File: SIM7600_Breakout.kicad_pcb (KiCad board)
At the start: 4 copper layers, 40 x 80 mm, 67 parts, among them J1 SIM8060-6-0-14-00-A, J2 2H header, J3 MJ-3502N, J4 30H Header, J5 USB_B_Micro, J6 U.FL-R-SMT-1(01), J7 U.FL-R-SMT-1(01), J8 U.FL-R-SMT-1(01), Q1 MMBT3904L_RFG, U1 NVT2008PW_118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

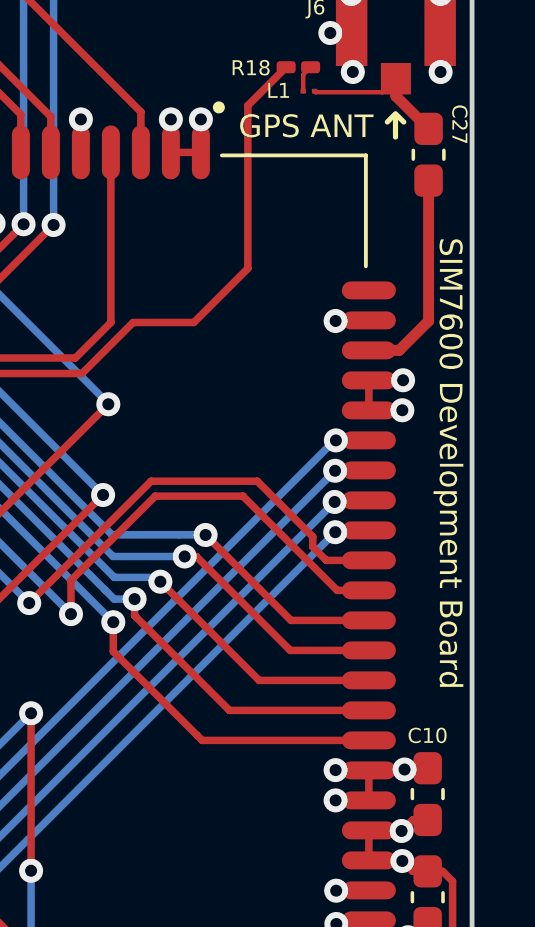
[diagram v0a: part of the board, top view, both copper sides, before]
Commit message: PCB label update
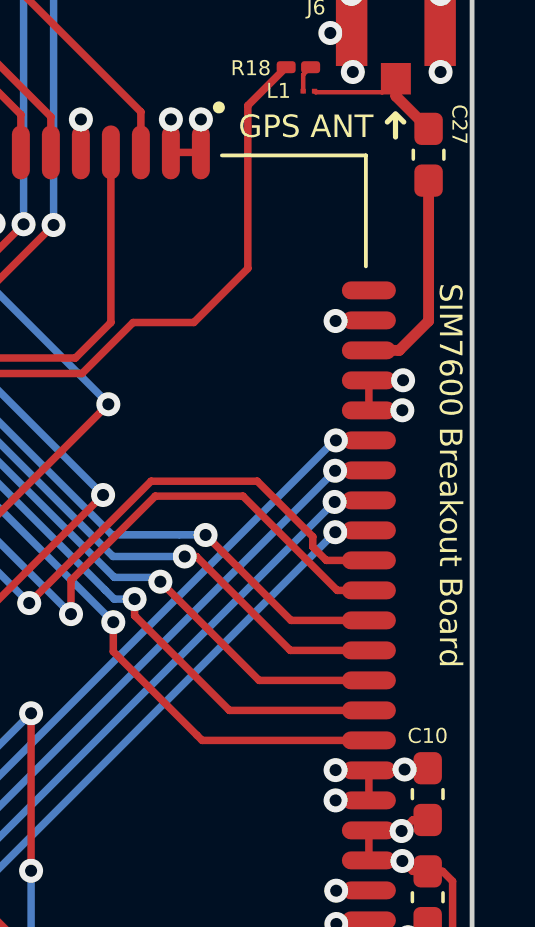
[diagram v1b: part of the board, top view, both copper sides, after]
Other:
- board text added: "SIM7600 Breakout Board"
- board text removed: "SIM7600 Development Board"
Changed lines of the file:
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@@
     (effects (font (size 0.5 0.5) (thickness 0.125)))
   )
-  (gr_text "SIM7600 Development Board" (at 158.275 100.3 270) (layer "F.SilkS")
+  (gr_text "SIM7600 Breakout Board" (at 158.275 100.7 270) (layer "F.SilkS")
     (effects (font (size 0.75 0.75) (thickness 0.15)))
   )

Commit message: Minor fixes
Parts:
- J2: value 2H header -> 2W Header
- J4: value 30H Header -> 30W Header
- U3: value SIM7600 -> SIM7600G-H
- turned R8 to 180 degrees
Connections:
- D3 pad C: /D+ -> /D-
- D4 pad C: /D- -> /D+
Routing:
- net /GPIO77: track 79.3 -> 78.3 mm
- net /+3v3: track 38.6 -> 37.7 mm
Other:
- rule pad_to_mask_clearance: 0 -> 0.0508
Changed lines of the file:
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@@
       (dielectric_constraints no)
     )
-    (pad_to_mask_clearance 0)
+    (pad_to_mask_clearance 0.0508)
     (pcbplotparams
       (layerselection 0x00010fc_ffffffff)
@@
       (effects (font (size 0.5 0.5) (thickness 0.075)))
     )
-    (fp_text value "SIM7600" (at -6.745 17.265 -270) (layer "F.Fab")
+    (fp_text value "SIM7600G-H" (at -6.745 17.265 -270) (layer "F.Fab")
       (effects (font (size 1 1) (thickness 0.15)))
     )
@@
       (effects (font (size 0.5 0.5) (thickness 0.075)))
     )
-    (fp_text value "2H header" (at 0 4.87 90) (layer "F.Fab")
+    (fp_text value "2W Header" (at 0 4.87 90) (layer "F.Fab")
       (effects (font (size 1 1) (thickness 0.15)))
     )
@@
       (net 2 "GND") (pintype "passive"))
     (pad "C" smd rect (at -0.58 0 90) (size 0.94 0.2) (layers "F.Cu" "F.Paste" "F.Mask")
-      (net 112 "/D-") (pintype "passive"))
+      (net 93 "/D+") (pintype "passive"))
     (model "${KIPRJMOD}/3dmodels/ESD9L5.0ST5G.step"
       (offset (xyz 0 0 0))
@@
       (net 2 "GND") (pintype "passive"))
     (pad "C" smd rect (at -0.58 0 90) (size 0.94 0.2) (layers "F.Cu" "F.Paste" "F.Mask")
-      (net 93 "/D+") (pintype "passive"))
+      (net 112 "/D-") (pintype "passive"))
     (model "${KIPRJMOD}/3dmodels/ESD9L5.0ST5G.step"
       (offset (xyz 0 0 0))
@@
   )
   (footprint "Resistor_SMD:R_0201_0603Metric_Pad0.64x0.40mm_HandSolder" (layer "F.Cu")
-    (at 125.0975 66.24)
+    (at 125.0975 66.24 180)
     (descr "Resistor SMD 0201 (0603 Metric), square (rectangular) end terminal, IPC_7351 nominal with elongated pad for handsoldering. (Body size source: https://www.vishay.com/docs/20052/crcw0201e3.pdf), generated with kicad-footprint-generator")
     (tags "resistor handsolder")
@@
     (property "Sheetname" "")
     (attr smd)
-    (fp_text reference "R8" (at 0 -0.665 unlocked) (layer "F.SilkS")
+    (fp_text reference "R8" (at 0 0.69 unlocked) (layer "F.SilkS")
       (effects (font (size 0.5 0.5) (thickness 0.075)))
     )
@@
     (fp_line (start -0.3 -0.15) (end 0.3 -0.15) (layer "F.Fab") (width 0.1))
     (fp_line (start -0.3 0.15) (end -0.3 -0.15) (layer "F.Fab") (width 0.1))
-    (pad "" smd roundrect (at -0.4325 0) (size 0.458 0.36) (layers "F.Paste") (roundrect_rratio 0.25))
-    (pad "" smd roundrect (at 0.4325 0) (size 0.458 0.36) (layers "F.Paste") (roundrect_rratio 0.25))
-    (pad "1" smd roundrect (at -0.4075 0) (size 0.635 0.4) (layers "F.Cu" "F.Mask") (roundrect_rratio 0.25)
+    (pad "" smd roundrect (at -0.4325 0 180) (size 0.458 0.36) (layers "F.Paste") (roundrect_rratio 0.25))
+    (pad "" smd roundrect (at 0.4325 0 180) (size 0.458 0.36) (layers "F.Paste") (roundrect_rratio 0.25))
+    (pad "1" smd roundrect (at -0.4075 0 180) (size 0.635 0.4) (layers "F.Cu" "F.Mask") (roundrect_rratio 0.25)
       (net 3 "Net-(Q1-Pad1)") (pintype "passive"))
-    (pad "2" smd roundrect (at 0.4075 0) (size 0.635 0.4) (layers "F.Cu" "F.Mask") (roundrect_rratio 0.25)
+    (pad "2" smd roundrect (at 0.4075 0 180) (size 0.635 0.4) (layers "F.Cu" "F.Mask") (roundrect_rratio 0.25)
       (net 90 "/PWR_ON") (pintype "passive"))
     (model "${KICAD6_3DMODEL_DIR}/Resistor_SMD.3dshapes/R_0201_0603Metric.wrl"
@@
       (effects (font (size 1 1) (thickness 0.15)) (justify mirror))
     )
-    (fp_text value "30H Header" (at 0 -75.99) (layer "B.Fab")
+    (fp_text value "30W Header" (at 0 -75.99) (layer "B.Fab")
       (effects (font (size 1 1) (thickness 0.15)) (justify mirror))
     )
@@
   (segment (start 154.985 87.21) (end 155.025 87.25) (width 0.3628) (layer "F.Cu") (net 2))
   (segment (start 157.55 70.465) (end 157.55 69.625) (width 0.25) (layer "F.Cu") (net 2))
-  (segment (start 155.6325 110.4575) (end 155.56 110.53) (width 0.25) (layer "F.Cu") (net 2))
   (segment (start 149.93 118.6) (end 148.96 118.6) (width 0.25) (layer "F.Cu") (net 2))
   (segment (start 132.96 120.13) (end 132.96 121.22) (width 0.25) (layer "F.Cu") (net 2))
@@
   (via (at 144.55 121.87) (size 0.8) (drill 0.4) (layers "F.Cu" "B.Cu") (net 2))
   (via (at 151.15 122.85) (size 0.8) (drill 0.4) (layers "F.Cu" "B.Cu") (net 2))
-  (segment (start 125.505 66.24) (end 125.505 67.1) (width 0.25) (layer "F.Cu") (net 3))
   (segment (start 125.505 67.1) (end 125.115 67.49) (width 0.25) (layer "F.Cu") (net 3))
+  (segment (start 125.505 66.24) (end 125.505 67.1) (width 0.25) (layer "F.Cu") (net 3))
   (segment (start 124.69 69.815) (end 125.115 69.39) (width 0.25) (layer "F.Cu") (net 4))
   (segment (start 124.69 70.615) (end 124.69 69.815) (width 0.25) (layer "F.Cu") (net 4))
@@
   (segment (start 142.899 125.178) (end 142.899 125.849) (width 0.25) (layer "F.Cu") (net 11))
   (segment (start 127.0985 87.0415) (end 127.06 87.08) (width 0.25) (layer "F.Cu") (net 11))
-  (segment (start 157.72 113.895) (end 157.4 113.575) (width 0.25) (layer "F.Cu") (net 11))
   (segment (start 125.246459 75.3825) (end 124.825 75.803959) (width 0.25) (layer "F.Cu") (net 11))
   (segment (start 157.0175 112.1825) (end 156.65 112.55) (width 0.25) (layer "F.Cu") (net 11))
@@
   (segment (start 124.77 113.53) (end 125.36 113.53) (width 0.25) (layer "F.Cu") (net 11))
   (segment (start 138.4015 127.98) (end 138.4015 127.8765) (width 0.25) (layer "F.Cu") (net 11))
-  (segment (start 155.56 113.53) (end 156.04 113.53) (width 0.18) (layer "F.Cu") (net 11))
   (segment (start 127.8375 86.869) (end 127.665 87.0415) (width 0.25) (layer "F.Cu") (net 11))
   (segment (start 124.825 76.940987) (end 124.910729 77.026716) (width 0.25) (layer "F.Cu") (net 11))
@@
   (segment (start 157.55 122.225) (end 157.2 121.875) (width 0.25) (layer "F.Cu") (net 15))
   (segment (start 137.05 92.225) (end 140.8 92.225) (width 0.25) (layer "F.Cu") (net 15))
-  (segment (start 145.965 116.245) (end 145.8175 116.3925) (width 0.25) (layer "F.Cu") (net 15))
   (segment (start 142.9065 122.548) (end 142.9065 122.0235) (width 0.2) (layer "F.Cu") (net 15))
   (segment (start 136.38975 135.463002) (end 136.006998 135.463002) (width 0.2) (layer "F.Cu") (net 15))
@@
   (segment (start 140.45 124.82) (end 139.79 124.16) (width 0.25) (layer "B.Cu") (net 17))
   (segment (start 145.5 117.875) (end 146.025 117.875) (width 0.25) (layer "B.Cu") (net 17))
-  (segment (start 145.412122 117.787122) (end 145.414744 117.7845) (width 0.25) (layer "B.Cu") (net 17))
   (segment (start 146.694598 101.35) (end 146.7 101.35) (width 0.25) (layer "B.Cu") (net 17))
   (segment (start 146.957299 118.607299) (end 146.225 117.875) (width 0.25) (layer "B.Cu") (net 17))
   (segment (start 145.96055 123.96945) (end 145.96055 121.219802) (width 0.25) (layer "B.Cu") (net 17))
-  (segment (start 145.412122 117.787122) (end 145.5 117.875) (width 0.25) (layer "B.Cu") (net 17))
   (segment (start 150.8 117.875) (end 157 124.075) (width 0.25) (layer "B.Cu") (net 17))
   (segment (start 137.495 124.445) (end 136.9105 124.445) (width 0.25) (layer "F.Cu") (net 18))
@@
   (segment (start 156.275 140.225) (end 156.275 118.5045) (width 0.25) (layer "F.Cu") (net 87))
   (segment (start 155.56 115.53) (end 154.595 115.53) (width 0.25) (layer "F.Cu") (net 87))
-  (segment (start 126.05 123.05) (end 126.05 124) (width 0.25) (layer "F.Cu") (net 87))
   (segment (start 126.05 124) (end 126.05 130.9) (width 0.25) (layer "F.Cu") (net 87))
-  (segment (start 155.5695 115.5205) (end 155.56 115.53) (width 0.25) (layer "F.Cu") (net 87))
   (segment (start 126.05 124) (end 125.025 122.975) (width 0.25) (layer "F.Cu") (net 87))
   (segment (start 125.025 122.975) (end 123.4 122.975) (width 0.25) (layer "F.Cu") (net 87))
@@
   (segment (start 127.35 142.18) (end 125.625 140.455) (width 0.25) (layer "F.Cu") (net 89))
   (segment (start 128.2875 142.18) (end 127.35 142.18) (width 0.25) (layer "F.Cu") (net 89))
-  (segment (start 124.69 66.24) (end 123.055 67.875) (width 0.25) (layer "F.Cu") (net 90))
   (segment (start 123.055 67.875) (end 121.65 67.875) (width 0.25) (layer "F.Cu") (net 90))
+  (segment (start 123.055 67.875) (end 124.69 66.24) (width 0.25) (layer "F.Cu") (net 90))
   (segment (start 136.38975 134.648002) (end 138.146998 134.648002) (width 0.3628) (layer "F.Cu") (net 91))
   (segment (start 138.146998 134.648002) (end 138.685 134.11) (width 0.3628) (layer "F.Cu") (net 91))
